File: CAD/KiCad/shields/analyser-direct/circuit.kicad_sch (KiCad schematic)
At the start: 1 part

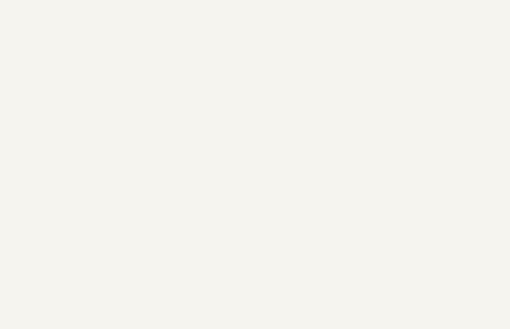
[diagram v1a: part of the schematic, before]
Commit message: Remove shield identification and adopt the simplified connector and Teensy pin maps
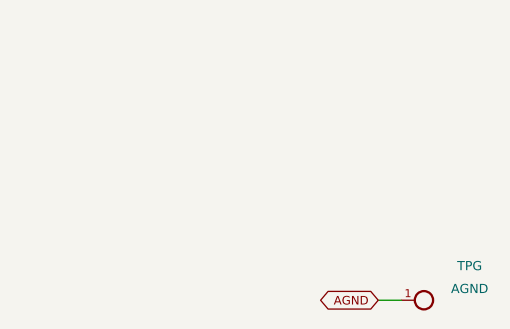
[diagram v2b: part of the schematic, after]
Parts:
- added TPG: AGND, Shields:TestPoint_Pad_D1.5mm, symbol Colloquy:TPG
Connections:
- new net AGND: TPG.1
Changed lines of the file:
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@@
 (wire (pts (xy 63.5000 50.8000) (xy 60.9600 50.8000)) (stroke (width 0) (type default)))
 (global_label "IOREF" (shape bidirectional) (at 60.9600 50.8000 180) (effects (font (size 0.95 0.95)) (justify right)) (property "Intersheetrefs" "${INTERSHEET_REFS}" (at 60.9600 50.8000 0) (effects (font (size 1.016 1.016))  (hide yes))))
+(symbol (lib_id "Colloquy:TPG") (at 195.5800 50.8000 0) (unit 1) (exclude_from_sim no) (in_bom no) (on_board yes) (dnp no)
+(property "Reference" "TPG" (at 200.6600 46.9900 0) (effects (font (size 1.016 1.016))  ))
+(property "Value" "AGND" (at 200.6600 49.5300 0) (effects (font (size 1.016 1.016))  ))
+(property "Footprint" "Shields:TestPoint_Pad_D1.5mm" (at 195.5800 50.8000 0) (effects (font (size 1.27 1.27))  (hide yes)))
+(property "Datasheet" "" (at 195.5800 50.8000 0) (effects (font (size 1.27 1.27))  (hide yes)))
+(property "Description" "" (at 195.5800 50.8000 0) (effects (font (size 1.27 1.27))  (hide yes)))
+(pin "1")
+(instances (project "analyser-direct" (path "/783c6f08-b3fb-5bc3-a49e-ea674f7f79b7/c6dafb66-03ac-5d57-8bf9-907fa23e9dee" (reference "TPG") (unit 1)))))
+(wire (pts (xy 193.0400 50.8000) (xy 190.5000 50.8000)) (stroke (width 0) (type default)))
+(global_label "AGND" (shape bidirectional) (at 190.5000 50.8000 180) (effects (font (size 0.95 0.95)) (justify right)) (property "Intersheetrefs" "${INTERSHEET_REFS}" (at 190.5000 50.8000 0) (effects (font (size 1.016 1.016))  (hide yes))))
           (embedded_fonts no))
